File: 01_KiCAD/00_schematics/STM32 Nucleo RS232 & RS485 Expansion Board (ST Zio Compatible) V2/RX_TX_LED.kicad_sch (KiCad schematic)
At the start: 24 parts, among them J4 HEADER 3POS 2.54mm, J5 HEADER 3POS 2.54mm, U3 SN74LVC2G14DBV

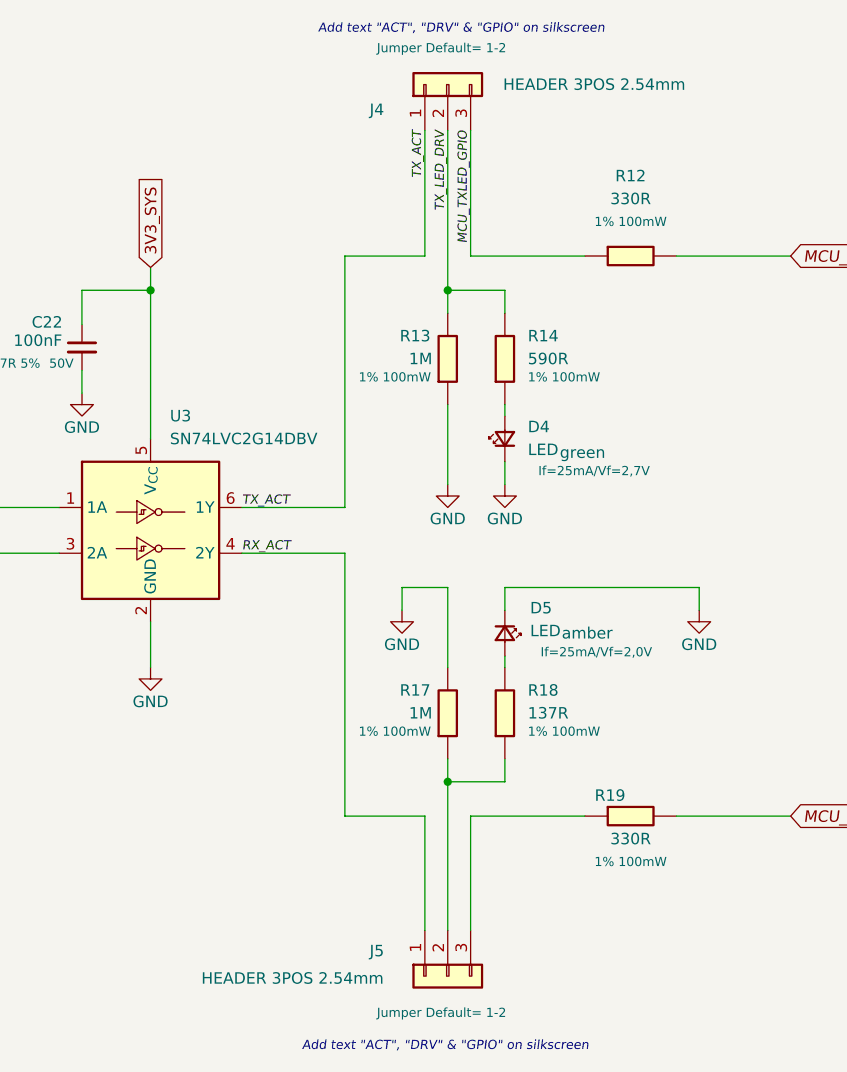
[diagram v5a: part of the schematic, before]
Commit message: Finishing up the schematic aand created the board outline
Made some finishing touches to the schematic, updated all the symbol footprints and started to create the board.
Added missing 3D models for Phoenix 4-p RS485 connector and RS232 connector, also for Inolux LED.
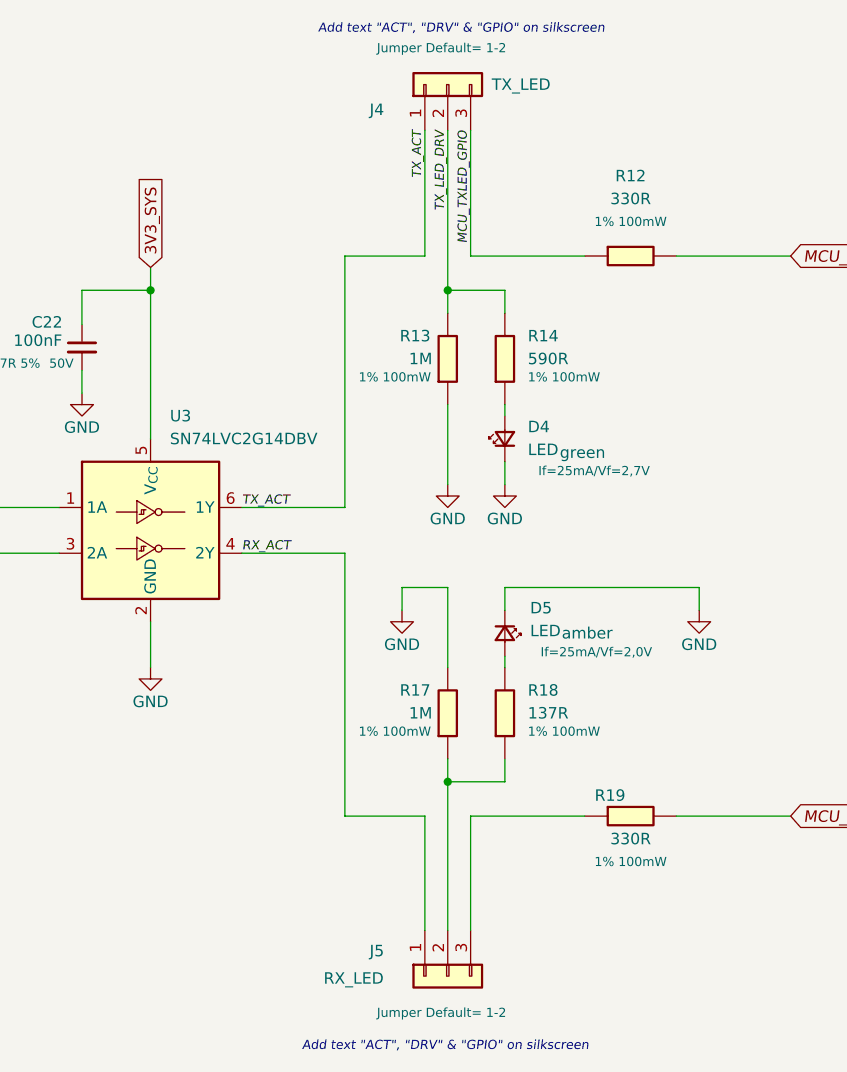
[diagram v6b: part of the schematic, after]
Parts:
- J4: value HEADER 3POS 2.54mm -> TX_LED; footprint (none) -> HTSW-103-07-F-S:CON3_1X3_TU_TSW
- J5: value HEADER 3POS 2.54mm -> RX_LED; footprint (none) -> HTSW-103-07-F-S:CON3_1X3_TU_TSW
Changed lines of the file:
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@@
 		(dnp no)
 		(fields_autoplaced yes)
-		(property "Reference" "#PWR028"
+		(property "Reference" "#PWR030"
 			(at 73.66 78.74 0)
 			(effects
@@
 			(project "STM32 Nucleo RS232 & RS485 Expansion Board (ST Zio Compatible) V2"
 				(path "/080f83b7-8913-48e8-ab8e-79cb12295542/d1bb9d55-41f4-4fc3-ae06-1adc98dc5d39"
-					(reference "#PWR028")
+					(reference "#PWR030")
 					(unit 1)
 				)
@@
 		(dnp no)
 		(fields_autoplaced yes)
-		(property "Reference" "#PWR035"
+		(property "Reference" "#PWR037"
 			(at 73.66 134.62 0)
 			(effects
@@
 			(project "STM32 Nucleo RS232 & RS485 Expansion Board (ST Zio Compatible) V2"
 				(path "/080f83b7-8913-48e8-ab8e-79cb12295542/d1bb9d55-41f4-4fc3-ae06-1adc98dc5d39"
-					(reference "#PWR035")
+					(reference "#PWR037")
 					(unit 1)
 				)
@@
 	)
 	(symbol
+		(lib_name "Conn_01x03_1")
 		(lib_id "Connector_Generic:Conn_01x03")
 		(at 173.99 35.56 90)
@@
 			)
 		)
-		(property "Value" "HEADER 3POS 2.54mm"
-			(at 200.406 35.56 90)
+		(property "Value" "TX_LED"
+			(at 185.42 35.56 90)
 			(effects
 				(font
@@
 			)
 		)
-		(property "Footprint" ""
+		(property "Footprint" "HTSW-103-07-F-S:CON3_1X3_TU_TSW"
 			(at 173.99 35.56 0)
 			(effects
@@
 			)
 		)
-		(property "Datasheet" "https://www.lcsc.com/datasheet/C6631883.pdf"
+		(property "Datasheet" "~"
 			(at 173.99 35.56 0)
 			(effects
@@
 			)
 		)
-		(property "Description" "Pin Header 3 Position 2.54mm Pitch Single Row Through Hole -55℃~+125℃"
+		(property "Description" "Generic connector, single row, 01x03, script generated (kicad-library-utils/schlib/autogen/connector/)"
 			(at 173.99 35.56 0)
 			(effects
@@
 		(dnp no)
 		(fields_autoplaced yes)
-		(property "Reference" "#PWR033"
+		(property "Reference" "#PWR035"
 			(at 201.93 100.33 0)
 			(effects
@@
 			(project "STM32 Nucleo RS232 & RS485 Expansion Board (ST Zio Compatible) V2"
 				(path "/080f83b7-8913-48e8-ab8e-79cb12295542/d1bb9d55-41f4-4fc3-ae06-1adc98dc5d39"
-					(reference "#PWR033")
+					(reference "#PWR035")
 					(unit 1)
 				)
@@
 		(dnp no)
 		(fields_autoplaced yes)
-		(property "Reference" "#PWR030"
+		(property "Reference" "#PWR032"
 			(at 173.99 86.36 0)
 			(effects
@@
 			(project "STM32 Nucleo RS232 & RS485 Expansion Board (ST Zio Compatible) V2"
 				(path "/080f83b7-8913-48e8-ab8e-79cb12295542/d1bb9d55-41f4-4fc3-ae06-1adc98dc5d39"
-					(reference "#PWR030")
+					(reference "#PWR032")
 					(unit 1)
 				)
@@
 		(dnp no)
 		(fields_autoplaced yes)
-		(property "Reference" "#PWR031"
+		(property "Reference" "#PWR033"
 			(at 180.34 86.36 0)
 			(effects
@@
 			(project "STM32 Nucleo RS232 & RS485 Expansion Board (ST Zio Compatible) V2"
 				(path "/080f83b7-8913-48e8-ab8e-79cb12295542/d1bb9d55-41f4-4fc3-ae06-1adc98dc5d39"
-					(reference "#PWR031")
+					(reference "#PWR033")
 					(unit 1)
 				)
@@
 		(dnp no)
 		(fields_autoplaced yes)
-		(property "Reference" "#PWR029"
+		(property "Reference" "#PWR031"
 			(at 90.17 78.74 0)
 			(effects
@@
 			(project "STM32 Nucleo RS232 & RS485 Expansion Board (ST Zio Compatible) V2"
 				(path "/080f83b7-8913-48e8-ab8e-79cb12295542/d1bb9d55-41f4-4fc3-ae06-1adc98dc5d39"
-					(reference "#PWR029")
+					(reference "#PWR031")
 					(unit 1)
 				)
@@
 		(dnp no)
 		(fields_autoplaced yes)
-		(property "Reference" "#PWR036"
+		(property "Reference" "#PWR038"
 			(at 90.17 134.62 0)
 			(effects
@@
 			(project "STM32 Nucleo RS232 & RS485 Expansion Board (ST Zio Compatible) V2"
 				(path "/080f83b7-8913-48e8-ab8e-79cb12295542/d1bb9d55-41f4-4fc3-ae06-1adc98dc5d39"
-					(reference "#PWR036")
+					(reference "#PWR038")
 					(unit 1)
 				)
@@
 		(dnp no)
 		(fields_autoplaced yes)
-		(property "Reference" "#PWR034"
+		(property "Reference" "#PWR036"
 			(at 140.97 106.68 0)
 			(effects
@@
 			(project "STM32 Nucleo RS232 & RS485 Expansion Board (ST Zio Compatible) V2"
 				(path "/080f83b7-8913-48e8-ab8e-79cb12295542/d1bb9d55-41f4-4fc3-ae06-1adc98dc5d39"
-					(reference "#PWR034")
+					(reference "#PWR036")
 					(unit 1)
 				)
@@
 			)
 		)
-		(property "Value" "HEADER 3POS 2.54mm"
+		(property "Value" "RX_LED"
 			(at 166.878 134.874 90)
 			(effects
@@
 			)
 		)
-		(property "Footprint" ""
+		(property "Footprint" "HTSW-103-07-F-S:CON3_1X3_TU_TSW"
 			(at 173.99 134.62 0)
 			(effects
@@
 			)
 		)
-		(property "Datasheet" "https://www.lcsc.com/datasheet/C6631883.pdf"
+		(property "Datasheet" "~"
 			(at 173.99 134.62 0)
 			(effects
@@
 			)
 		)
-		(property "Description" "Pin Header 3 Position 2.54mm Pitch Single Row Through Hole -55℃~+125℃"
+		(property "Description" "Generic connector, single row, 01x03, script generated (kicad-library-utils/schlib/autogen/connector/)"
 			(at 173.99 134.62 0)
 			(effects
@@
 		(dnp no)
 		(fields_autoplaced yes)
-		(property "Reference" "#PWR032"
+		(property "Reference" "#PWR034"
 			(at 168.91 100.33 0)
 			(effects
@@
 			(project "STM32 Nucleo RS232 & RS485 Expansion Board (ST Zio Compatible) V2"
 				(path "/080f83b7-8913-48e8-ab8e-79cb12295542/d1bb9d55-41f4-4fc3-ae06-1adc98dc5d39"
-					(reference "#PWR032")
+					(reference "#PWR034")
 					(unit 1)
 				)
@@
 		(dnp no)
 		(fields_autoplaced yes)
-		(property "Reference" "#PWR027"
+		(property "Reference" "#PWR029"
 			(at 133.35 76.2 0)
 			(effects
@@
 			(project "STM32 Nucleo RS232 & RS485 Expansion Board (ST Zio Compatible) V2"
 				(path "/080f83b7-8913-48e8-ab8e-79cb12295542/d1bb9d55-41f4-4fc3-ae06-1adc98dc5d39"
-					(reference "#PWR027")
+					(reference "#PWR029")
 					(unit 1)
 				)

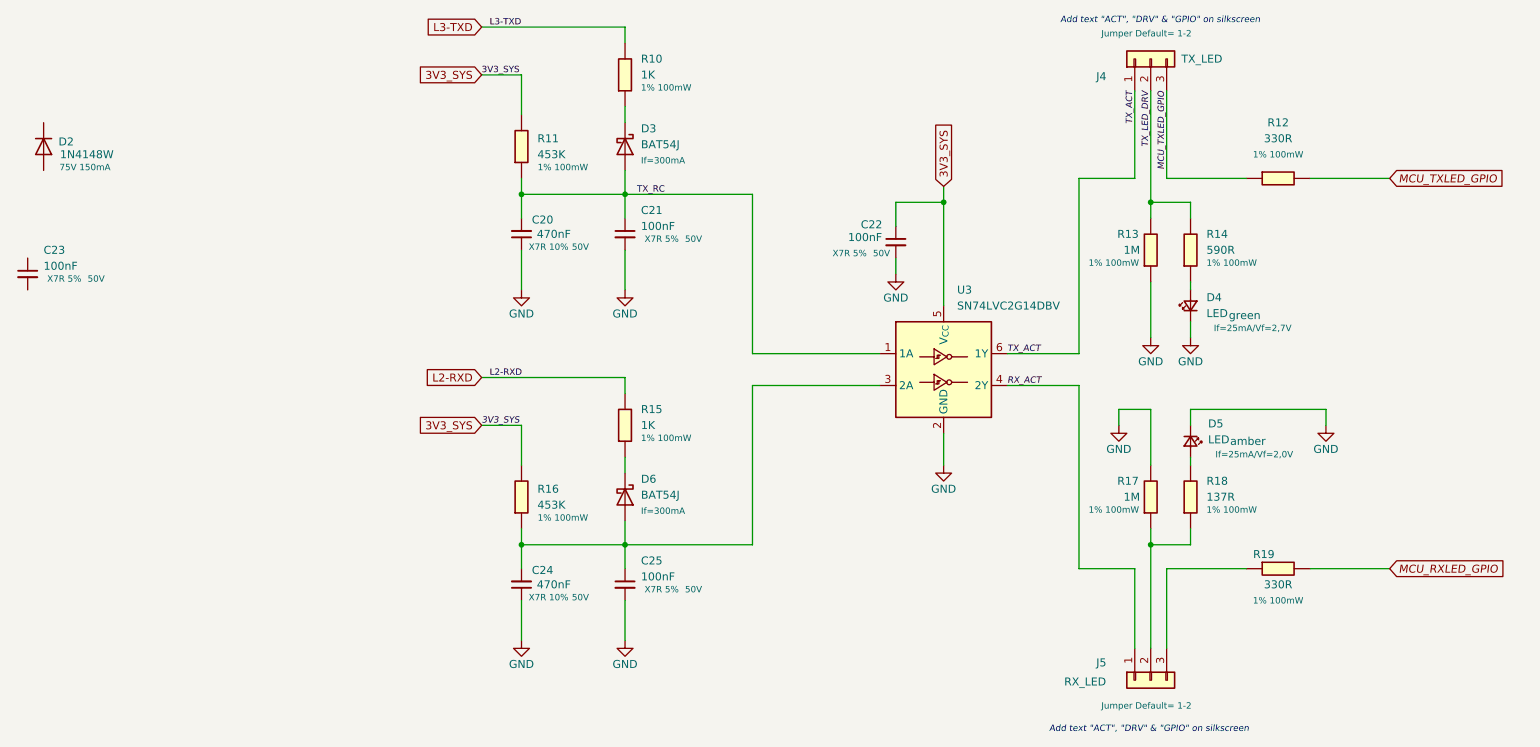
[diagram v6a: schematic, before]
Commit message: Updated footprints and added components to PCB
Added some additional components to the board. Changed the footprint of the 3-pin Jumper so the bottom silkscreen text doesnlt overlap with the Dual Schmidt Trigger IC's SN74LVC2G14
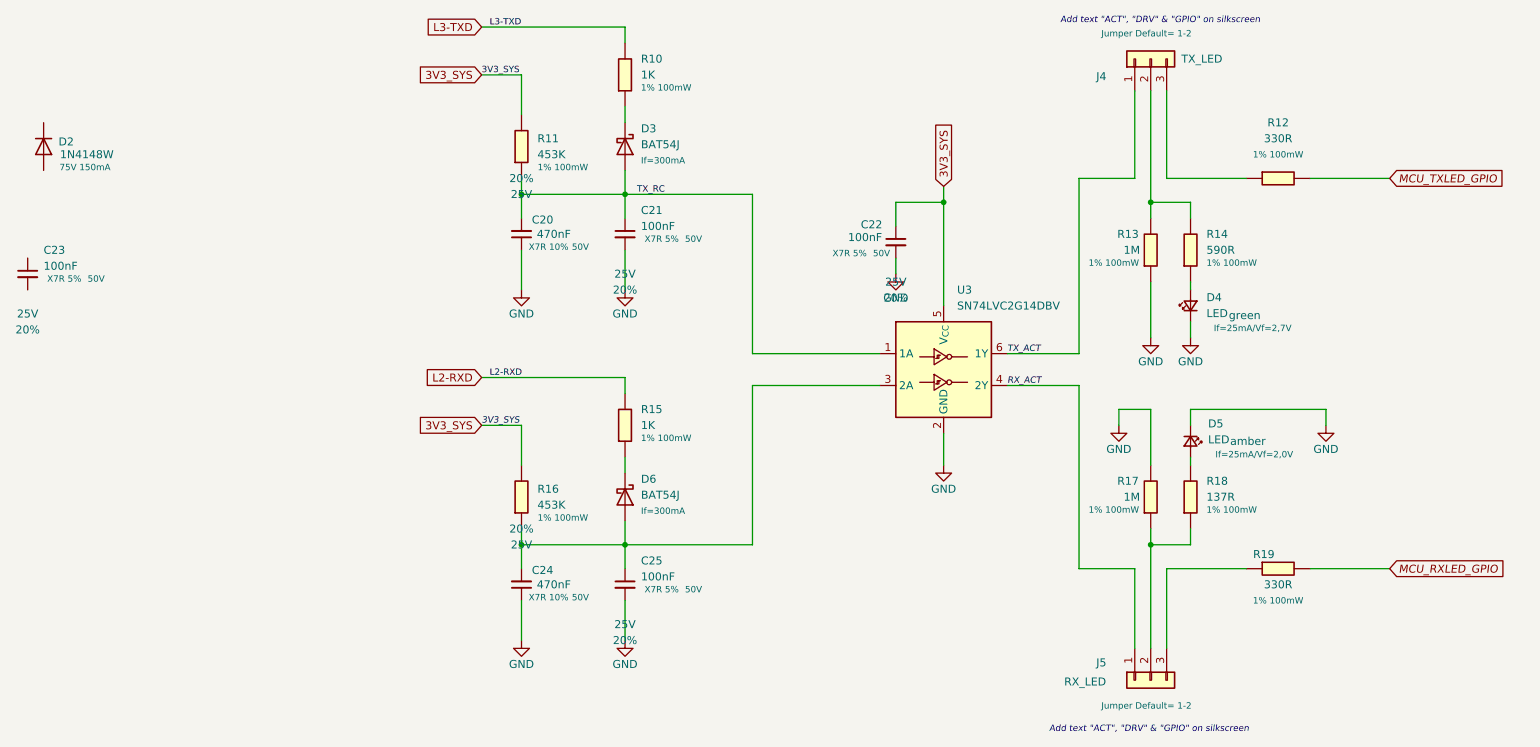
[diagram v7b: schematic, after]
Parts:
- C20, C21, C22, C23, C24, C25: PROD_ID (none) -> CAP-00810; Tolerance (none) -> 20%; Voltage (none) -> 25V
- J4, J5: footprint HTSW-103-07-F-S:CON3_1X3_TU_TSW -> Samtec_Connector:Samtec HTSW-103-07-F-S
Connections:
- net MCU_TXLED_GPIO: no longer J4.3 (Pin_3), R12.2
- net TX_LED_DRV: no longer names the net of J4.2 (Pin_2), R13.1, R14.1
- new net: J4.3 (Pin_3), R12.2

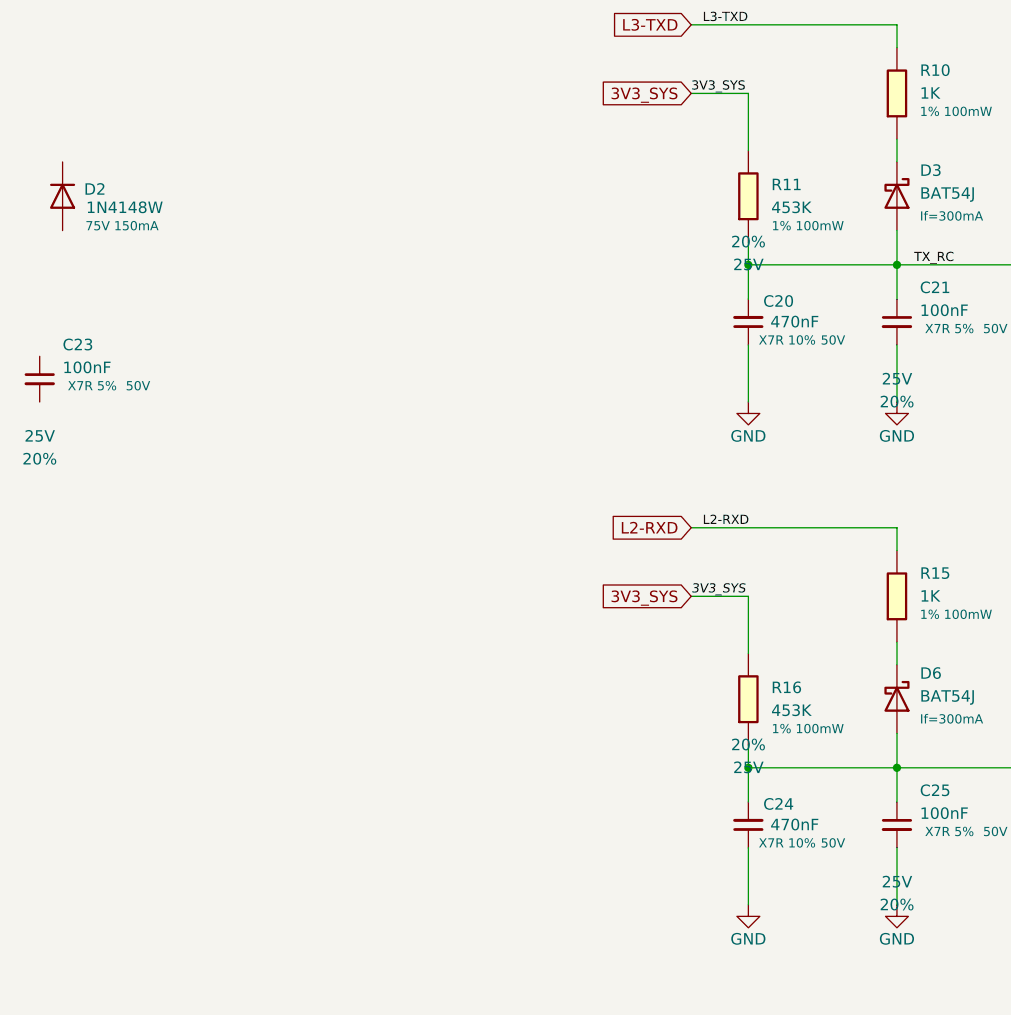
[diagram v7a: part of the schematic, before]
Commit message: Changed schmitt trigger
changed the schmitt trigger for hex-schmitt trigger variant to simpify design and reduce components
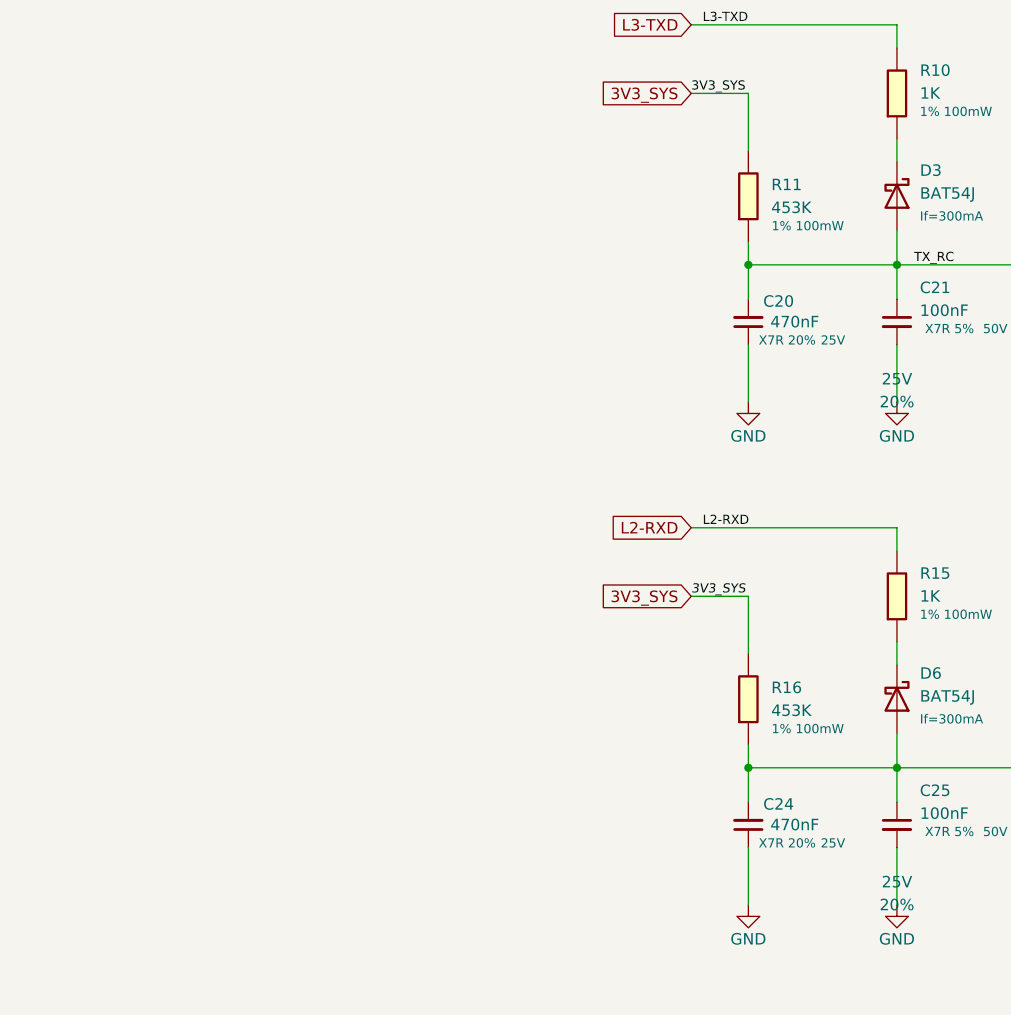
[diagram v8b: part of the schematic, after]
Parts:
- removed C23: 100nF, PCM_SparkFun-Capacitor:C_0603_1608Metric, symbol PCM_SparkFun-Capacitor:0.1uF_0603_25V_20%
- removed D2: 1N4148W, Diode_SMD:D_SOD-123, symbol Diode:1N4148W
- C20, C24: Dielectric X7R 10% -> X7R 20%; Voltage Rating 50V -> 25V
